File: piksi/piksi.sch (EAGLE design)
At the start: 156 parts, among them J1 SMA_EDGE, J6 ZX62-B-5PA, Q1 IRLML6401, U1 6SLX9FTG256, U10 MAX2769, U12 PT7M8206B33TA5EX, U13 M25PX80, U2 LTC3407A_DFN, U3 STM32-M-64-LQFP, U4 7Q-16.368MBG-T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

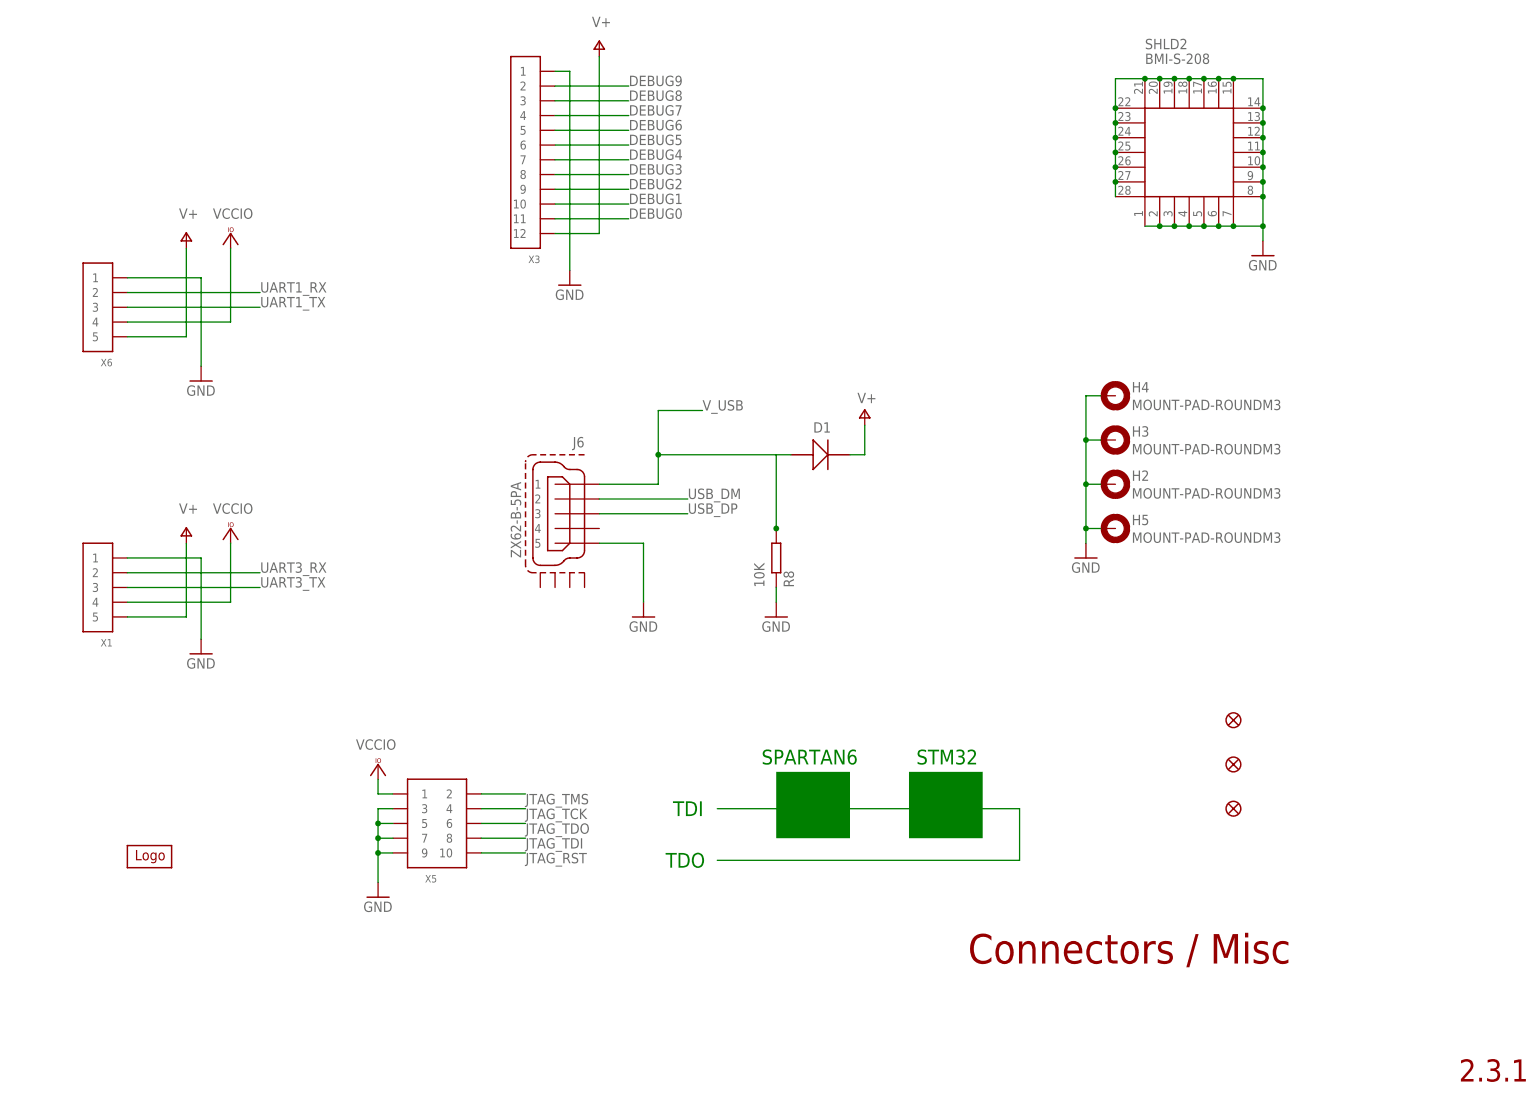
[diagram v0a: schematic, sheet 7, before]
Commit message: Changed frame, description, and added copyright/license notice for sheet 7
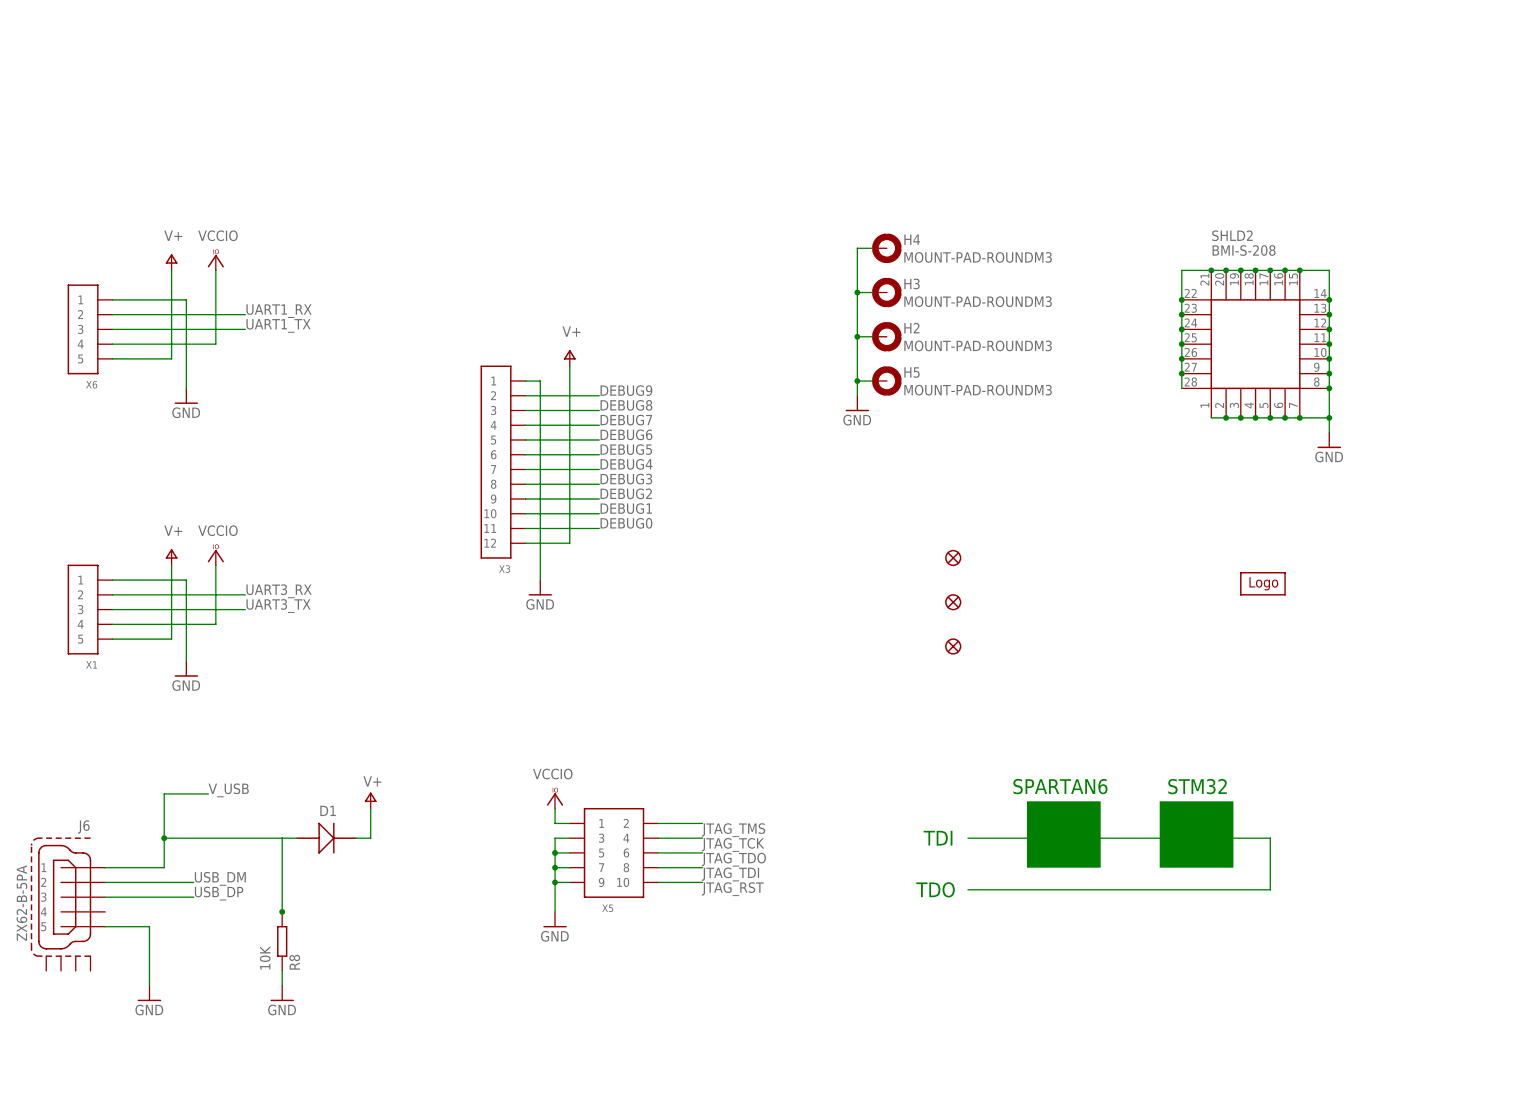
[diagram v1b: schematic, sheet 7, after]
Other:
- note added: "Copyright (C) 2011-2013 Swift Navigation Inc."
- note added: "License : CC BY-SA 3.0"
- note added: "Piksi 2.3.1"
- note added: "v2.3.1"
- moved on the sheet: D1, H2, H3, H4, H5, J6, R8, SHLD2, X1, X3, X5, X6

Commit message: Changed frame, description, and added copyright/license notice for sheet 6
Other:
- note added: "FTDI UART / FIFO to USB"
- note removed: "FTDI UART/FIFO to USB"
- moved on the sheet: C34, C35, C45, C49, C50, C56, C57, C58, C59, C64, C65, C68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

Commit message: Changed frame, description, and added copyright/license notice for sheet 5
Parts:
- L1: value 27nH / DNP -> DNP
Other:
- note added: "Digital Power Rails"
- note removed: "Digital Power"
- moved on the sheet: C1, C2, C3, C4, C5, L13, L14, Q1, R1, R61, R62, R63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

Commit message: Changed frame, description, and added copyright/license notice for sheet 4
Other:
- note added: "RF Frontend - Power Pins"
- note removed: "RF Frontend - Power"
- moved on the sheet: C107, C11, C12, C13, C14, C15, C16, C18, C19, C20, C36, C37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

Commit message: Changed frame, description, and added copyright/license notice for sheet 3
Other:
- moved on the sheet: C10, C17, C21, C22, C23, C24, C25, C26, C28, C29, C30, C31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
